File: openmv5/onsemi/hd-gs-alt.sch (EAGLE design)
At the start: 54 parts, among them IC1 AR0135CS2C00SUEA0, IC2 TLV62568PDDCR, IC3 MIC5365-2.8YC5-TR, J1 DF12-36-DP, Q1 PMXB120EPEZ

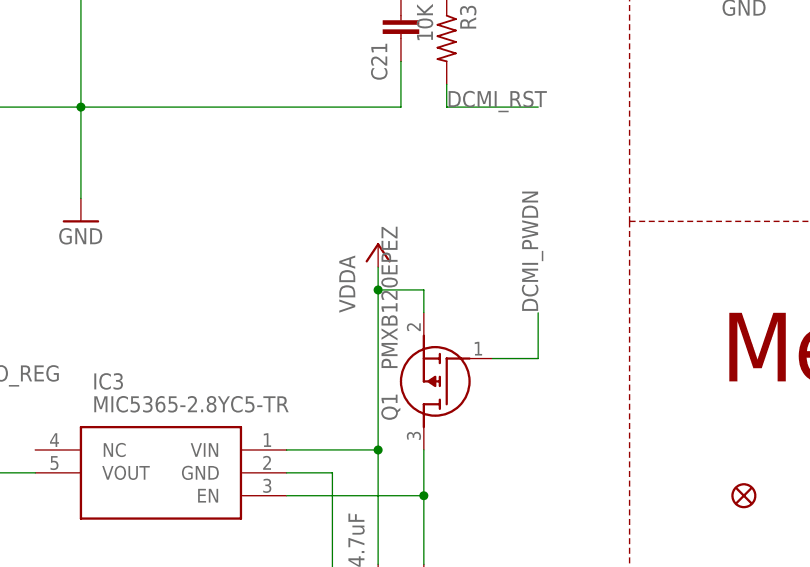
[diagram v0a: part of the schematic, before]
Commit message: Update camera modules to use different non-flippable pmosfet
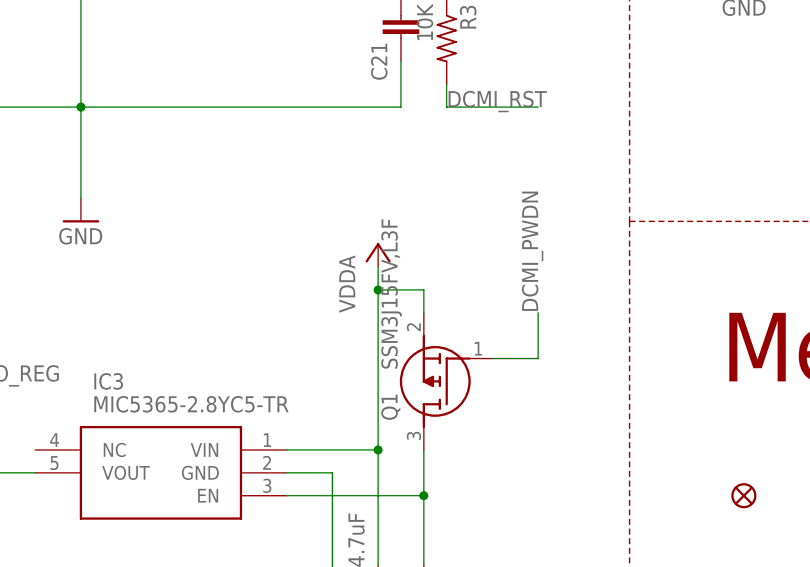
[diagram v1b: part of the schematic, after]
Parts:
- Q1: value PMXB120EPEZ -> SSM3J15FV,L3F; device PMXB120EPEZ:PMXB120EPEZ -> SSM3J15FV_L3F:SSM3J15FV,L3F; MPN PMXB120EPEZ -> SSM3J15FV,L3F
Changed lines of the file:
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@@
 </part>
 <part name="GND11" library="supply" deviceset="GND" device=""/>
-<part name="Q1" library="PMXB120EPEZ" deviceset="PMXB120EPEZ" device="">
-<attribute name="MPN" value="PMXB120EPEZ"/>
+<part name="Q1" library="SSM3J15FV_L3F" deviceset="SSM3J15FV,L3F" device="">
+<attribute name="MPN" value="SSM3J15FV,L3F"/>
 </part>
 <part name="R4" library="rcl" library_urn="urn:adsk.eagle:library:334" deviceset="R-US_" device="R0402" package3d_urn="urn:adsk.eagle:package:23547/3" value="100K">
